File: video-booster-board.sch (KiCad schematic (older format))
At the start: 129 parts, among them IC1 INA180A1IDBVT, J1 0473460001, J10 M20-9990246, J11 MC-HVT1-S04-G, J2 HDMI-PE10-19-LF, J3 HDMI-PE10-19-LF, J6 685119134923_, J9 685119134923_, SW1 1571983-5, U1 PTN3363, U2 TPS2110APW, U3 PTN3363, U4 LP2985-33DBVR, U5 NTS0102GT, U6 EFM32HG321, U7 NTS0102GT

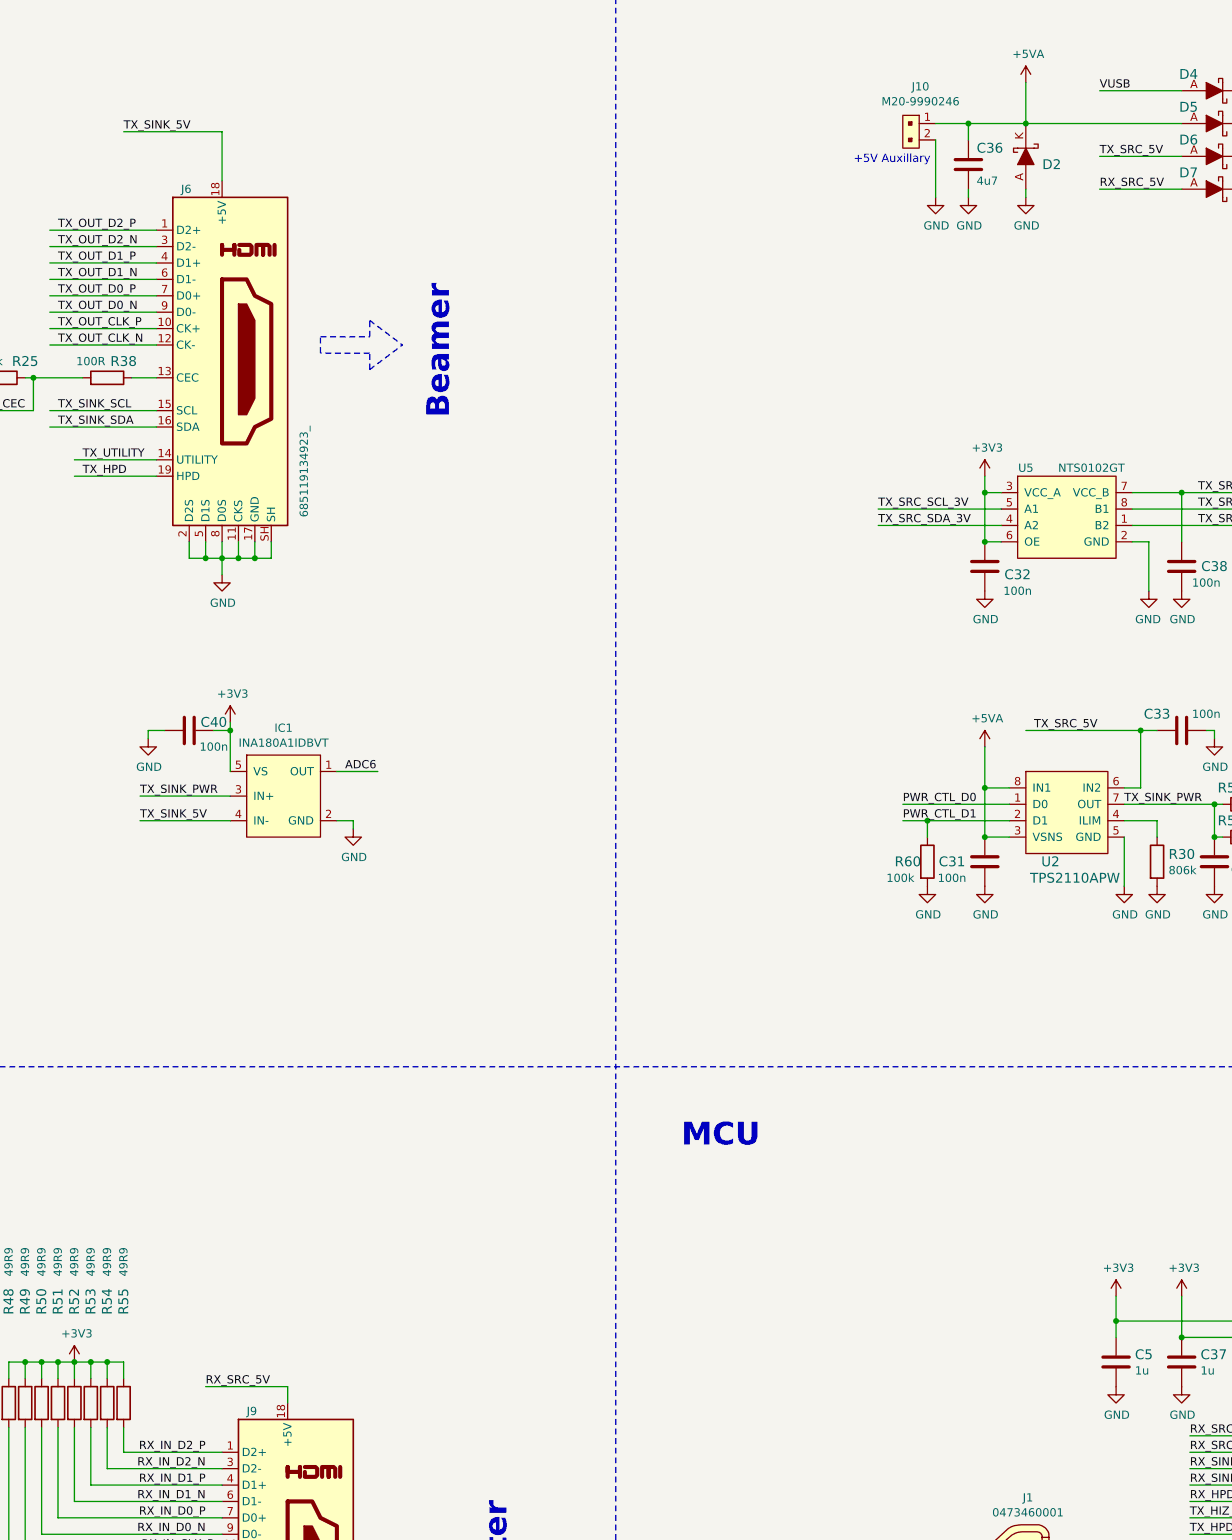
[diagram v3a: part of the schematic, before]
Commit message: Additional decoupling on MCU adn TX_SINK_5V added
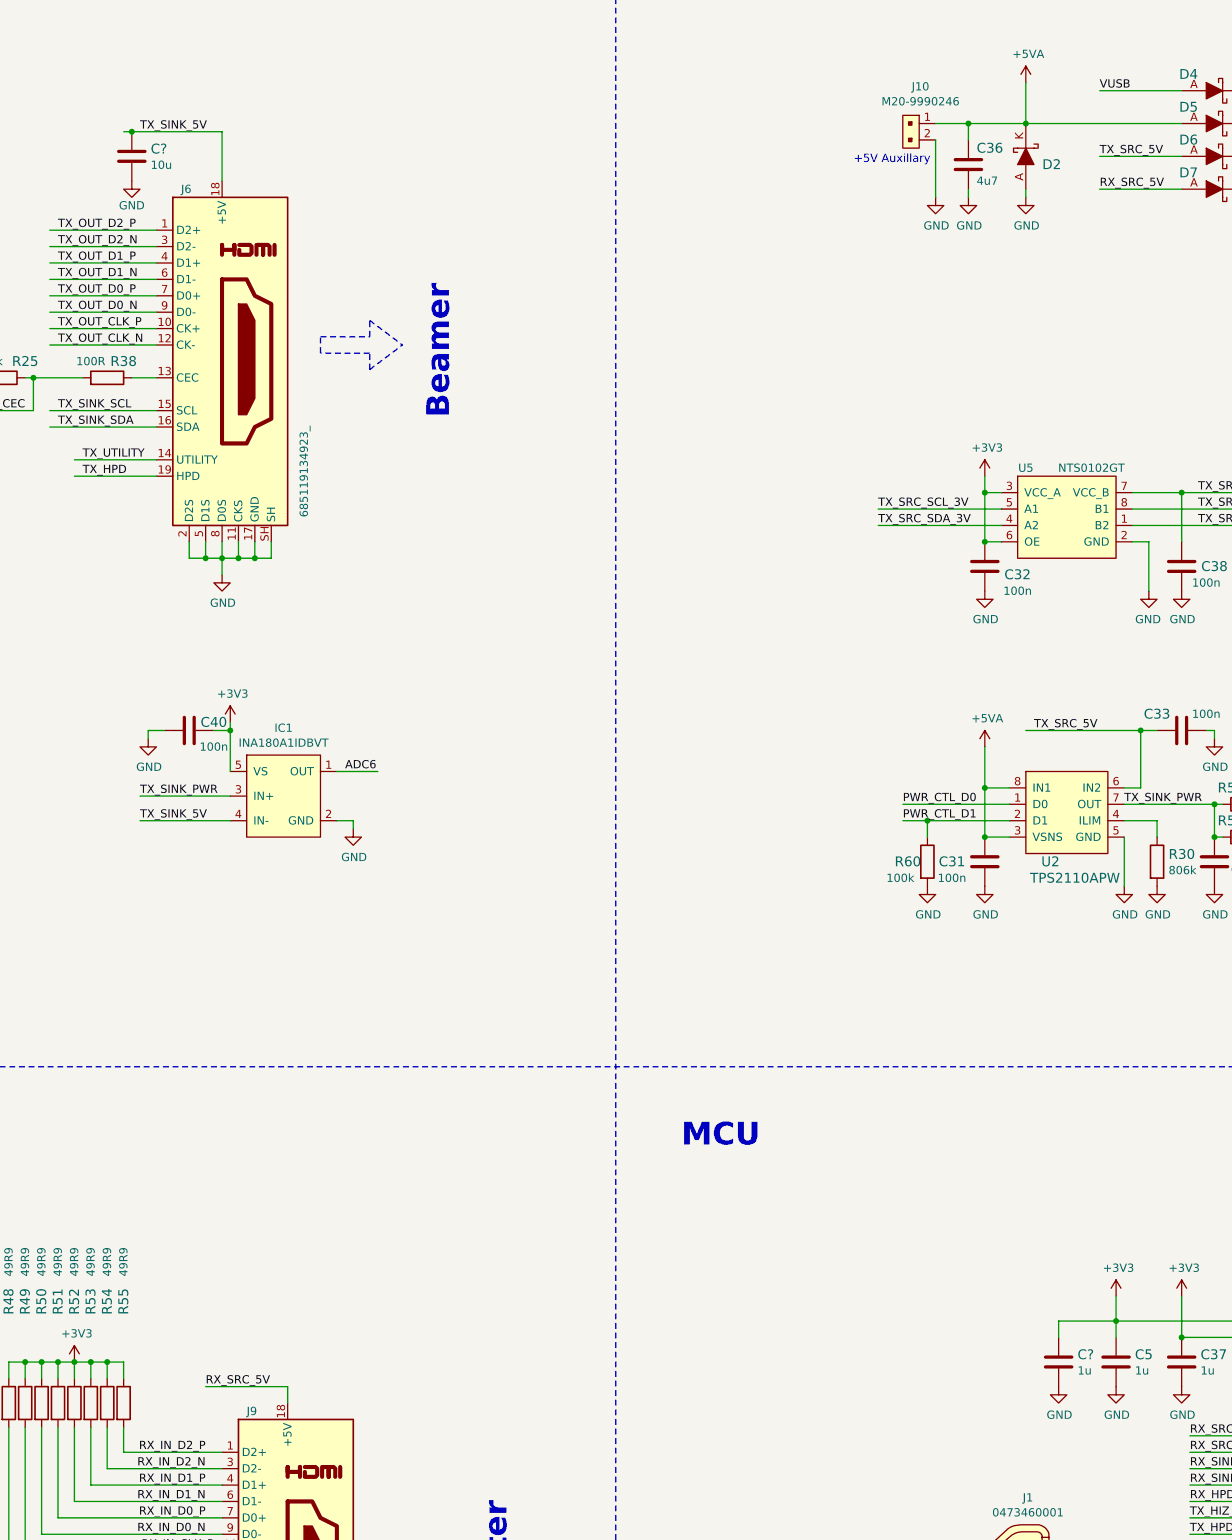
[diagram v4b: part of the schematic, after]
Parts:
- added C?: C_1u_0402, video-booster-board-footprints:0402-cap, symbol video-booster-board:C_1u_0402-
- added C?: C_10u_0603, video-booster-board-footprints:0603-cap, symbol video-booster-board:C_10u_0603-
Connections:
- wire segments 564 -> 567
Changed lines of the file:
@@
 Wire Wire Line
 	16800 5950 17350 5950
-Text Label 9750 1850 0    50   ~ 0
+Text Label 9850 1850 0    50   ~ 0
 TX_SINK_5V
 Wire Wire Line
-	10350 1850 9750 1850
+	10350 1850 9800 1850
 Wire Notes Line
 	12800 13000 22950 13000
@@
 Wire Wire Line
 	16850 10300 16250 10300
+$Comp
+L video-booster-board:C_1u_0402- C?
+U 1 1 5DE6659D
+P 15450 9350
+F 0 "C?" H 15565 9395 60  0000 L CNN
+F 1 "C_1u_0402" H 15450 9200 60  0001 C CNN
+F 2 "video-booster-board-footprints:0402-cap" H 15650 9550 60  0001 L CNN
+F 3 "" H 15450 9350 50  0001 C CNN
+F 4 "TDK" H 15650 9750 60  0001 L CNN "Manufacturer"
+F 5 "C1005X6S1A105K050BC" H 15650 9650 60  0001 L CNN "MPN"
+F 6 "1u" H 15565 9297 50  0000 L CNN "Val"
+	1    15450 9350
+	1    0    0    -1
+$EndComp
+$Comp
+L video-booster-board:GND #PWR?
+U 1 1 5DE668F7
+P 15450 9500
+F 0 "#PWR?" H 15450 9250 50  0001 C CNN
+F 1 "GND" H 15455 9327 50  0000 C CNN
+F 2 "" H 15450 9500 50  0001 C CNN
+F 3 "" H 15450 9500 50  0001 C CNN
+	1    15450 9500
+	1    0    0    -1
+$EndComp
+Wire Wire Line
+	15800 9100 15450 9100
+Wire Wire Line
+	15450 9100 15450 9200
+$Comp
+L video-booster-board:C_10u_0603- C?
+U 1 1 5DED3A14
+P 9800 2000
+F 0 "C?" H 9915 2045 60  0000 L CNN
+F 1 "C_10u_0603" H 9800 1850 60  0001 C CNN
+F 2 "video-booster-board-footprints:0603-cap" H 10000 2200 60  0001 L CNN
+F 3 "" H 9800 2000 50  0001 C CNN
+F 4 "AVX" H 10000 2400 60  0001 L CNN "Manufacturer"
+F 5 "06036D106MAT2A" H 10000 2300 60  0001 L CNN "MPN"
+F 6 "10u" H 9915 1947 50  0000 L CNN "Val"
+	1    9800 2000
+	1    0    0    -1
+$EndComp
+Connection ~ 9800 1850
+Wire Wire Line
+	9800 1850 9750 1850
+$Comp
+L video-booster-board:GND #PWR?
+U 1 1 5DED892B
+P 9800 2150
+F 0 "#PWR?" H 9800 1900 50  0001 C CNN
+F 1 "GND" H 9800 2000 50  0000 C CNN
+F 2 "" H 9800 2150 50  0001 C CNN
+F 3 "" H 9800 2150 50  0001 C CNN
+	1    9800 2150
+	1    0    0    -1
+$EndComp
 $EndSCHEMATC

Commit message: OSHW logo and board name added on PCB
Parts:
- added N1: oshw_logo, video-booster-board-footprints:OSHW-Logo2_7.3x6mm_Copper_Mask, symbol video-booster-board:oshw_logo
- gave numbers to parts that had none: 2
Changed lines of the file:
@@
 TX_HIZ_EN
 $Bitmap
-Pos 2300 15650
+Pos 19400 15100
 Scale 1.000000
 Data
@@
 RX_SINK_CEC
 $Bitmap
-Pos 1100 15650
+Pos 22500 15100
 Scale 0.850000
 Data
@@
 	16850 10300 16250 10300
 $Comp
-L video-booster-board:C_1u_0402- C?
+L video-booster-board:C_1u_0402- C42
 U 1 1 5DE6659D
 P 15450 9350
-F 0 "C?" H 15565 9395 60  0000 L CNN
+F 0 "C42" H 15565 9395 60  0000 L CNN
 F 1 "C_1u_0402" H 15450 9200 60  0001 C CNN
 F 2 "video-booster-board-footprints:0402-cap" H 15650 9550 60  0001 L CNN
@@
 $EndComp
 $Comp
-L video-booster-board:GND #PWR?
+L video-booster-board:GND #PWR026
 U 1 1 5DE668F7
 P 15450 9500
-F 0 "#PWR?" H 15450 9250 50  0001 C CNN
+F 0 "#PWR026" H 15450 9250 50  0001 C CNN
 F 1 "GND" H 15455 9327 50  0000 C CNN
 F 2 "" H 15450 9500 50  0001 C CNN
@@
 	15450 9100 15450 9200
 $Comp
-L video-booster-board:C_10u_0603- C?
+L video-booster-board:C_10u_0603- C41
 U 1 1 5DED3A14
 P 9800 2000
-F 0 "C?" H 9915 2045 60  0000 L CNN
+F 0 "C41" H 9915 2045 60  0000 L CNN
 F 1 "C_10u_0603" H 9800 1850 60  0001 C CNN
 F 2 "video-booster-board-footprints:0603-cap" H 10000 2200 60  0001 L CNN
@@
 	9800 1850 9750 1850
 $Comp
-L video-booster-board:GND #PWR?
+L video-booster-board:GND #PWR021
 U 1 1 5DED892B
 P 9800 2150
-F 0 "#PWR?" H 9800 1900 50  0001 C CNN
+F 0 "#PWR021" H 9800 1900 50  0001 C CNN
 F 1 "GND" H 9800 2000 50  0000 C CNN
 F 2 "" H 9800 2150 50  0001 C CNN
@@
 	1    0    0    -1
 $EndComp
+$Comp
+L video-booster-board:oshw_logo N1
+U 1 1 5DF48A15
+P 22350 13450
+F 0 "N1" H 22100 13800 50  0000 L CNN
+F 1 "oshw_logo" H 22100 13700 50  0000 L CNN
+F 2 "video-booster-board-footprints:OSHW-Logo2_7.3x6mm_Copper_Mask" H 22250 13700 50  0001 C CNN
+F 3 "" H 22350 13800 50  0001 C CNN
+	1    22350 13450
+	1    0    0    -1
+$EndComp

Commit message: Updated sections
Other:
- note added: "Markings"
- note added: "TBD: Consider changing into a small barrel jack (SMT)"
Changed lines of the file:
@@
 TX_HIZ_EN
 $Bitmap
-Pos 19400 15100
+Pos 1400 15650
 Scale 1.000000
 Data
@@
 	1    0    0    -1
 $EndComp
-Text Notes 14200 2050 0    50   ~ 0
+Text Notes 14000 1850 0    50   ~ 0
 +5V Auxillary
 $Comp
@@
 RX_SINK_CEC
 $Bitmap
-Pos 22500 15100
+Pos 2600 15650
 Scale 0.850000
 Data
@@
 L video-booster-board:oshw_logo N1
 U 1 1 5DF48A15
-P 22350 13450
-F 0 "N1" H 22100 13800 50  0000 L CNN
-F 1 "oshw_logo" H 22100 13700 50  0000 L CNN
-F 2 "video-booster-board-footprints:OSHW-Logo2_7.3x6mm_Copper_Mask" H 22250 13700 50  0001 C CNN
-F 3 "" H 22350 13800 50  0001 C CNN
-	1    22350 13450
+P 18900 14250
+F 0 "N1" H 18650 14600 50  0000 L CNN
+F 1 "oshw_logo" H 18650 14500 50  0000 L CNN
+F 2 "video-booster-board-footprints:OSHW-Logo2_7.3x6mm_Copper_Mask" H 18800 14500 50  0001 C CNN
+F 3 "" H 18900 14600 50  0001 C CNN
+	1    18900 14250
 	1    0    0    -1
 $EndComp
+Text Notes 13600 2650 0    50   ~ 0
+TBD: Consider changing into a small barrel jack (SMT)
+Wire Notes Line
+	17650 13000 17650 16050
+Text Notes 17800 13350 0    138  ~ 28
+Markings
 $EndSCHEMATC

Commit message: Opsis side HDMI connector type changed. Board shape adjusted, DC jack added
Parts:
- removed J2, J3: HDMI-PE10-19-LF, video-booster-board-footprints:HDMI-PE10-19-LF, symbol video-booster-board:HDMI-PE10-19-LF-
- removed J6, J9: 685119134923_, video-booster-board-footprints:HDMI_A_Female_685119134923, symbol video-booster-board:685119134923_-
- added J2, J3: CHDMI-AMSS-01-C, video-booster-board-footprints:CHDMI-AMSS-01-C, symbol video-booster-board:CHDMI-AMSS-01-C
- added J4: 694103107102, video-booster-board-footprints:69410X107102, symbol video-booster-board:694103107102
- added J6, J9: 685119134923_, video-booster-board-footprints:HDMI_A_Female_685119134923, symbol video-booster-board:685119134923_
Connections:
- wire segments 567 -> 572
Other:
- note removed: "TBD: Consider changing into a small barrel jack (SMT)"
- moved on the sheet: J10
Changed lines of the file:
@@
 $EndComp
 $Comp
-L video-booster-board:HDMI-PE10-19-LF- J2
-U 1 1 5DBAED87
-P 2100 3400
-F 0 "J2" V 1650 2650 50  0000 R CNN
-F 1 "HDMI-PE10-19-LF" V 1750 3300 50  0000 R CNN
-F 2 "video-booster-board-footprints:HDMI-PE10-19-LF" H 2300 3600 60  0001 L CNN
-F 3 "http://www.morethanall.com/images/products/March2017/JtPYSqVaIFqwSbTYDg6j.pdf" H 2175 3550 50  0001 C CNN
-	1    2100 3400
-	1    0    0    -1
-$EndComp
-$Comp
-L video-booster-board:685119134923_- J6
-U 1 1 5DBAFB0A
-P 10350 3250
-F 0 "J6" H 10100 4300 50  0000 L CNN
-F 1 "685119134923_" V 10850 2300 50  0000 L CNN
-F 2 "video-booster-board-footprints:HDMI_A_Female_685119134923" H 10550 3450 60  0001 L CNN
-F 3 "https://katalog.we-online.de/em/datasheet/685119134923.pdf" H 10375 3250 50  0001 C CNN
-	1    10350 3250
-	1    0    0    -1
-$EndComp
-$Comp
 L video-booster-board:C_100n_0402_6V3- C27
 U 1 1 5DBDC1F8
@@
 $EndComp
 $Comp
-L video-booster-board:HDMI-PE10-19-LF- J3
-U 1 1 5DF9B9E7
-P 2450 10850
-F 0 "J3" V 2000 10100 50  0000 R CNN
-F 1 "HDMI-PE10-19-LF" V 2100 10750 50  0000 R CNN
-F 2 "video-booster-board-footprints:HDMI-PE10-19-LF" H 2650 11050 60  0001 L CNN
-F 3 "http://www.morethanall.com/images/products/March2017/JtPYSqVaIFqwSbTYDg6j.pdf" H 2525 11000 50  0001 C CNN
-	1    2450 10850
-	1    0    0    -1
-$EndComp
-$Comp
-L video-booster-board:685119134923_- J9
-U 1 1 5DF9B9EE
-P 10750 10700
-F 0 "J9" H 10500 11750 50  0000 L CNN
-F 1 "685119134923_" V 11250 9750 50  0000 L CNN
-F 2 "video-booster-board-footprints:HDMI_A_Female_685119134923" H 10950 10900 60  0001 L CNN
-F 3 "https://katalog.we-online.de/em/datasheet/685119134923.pdf" H 10775 10700 50  0001 C CNN
-	1    10750 10700
-	1    0    0    -1
-$EndComp
-$Comp
 L video-booster-board:PTN3363- U1
 U 1 1 5DF9BA02
@@
 TX_SINK_SCL_3V
 $Comp
-L video-booster-board:C_4u7_0603- C36
-U 1 1 62A47AFC
-P 14900 2050
-F 0 "C36" H 14950 2150 60  0000 L CNN
-F 1 "C_4u7_0603" H 14900 1900 60  0001 C CNN
-F 2 "video-booster-board-footprints:0603-cap" H 15100 2250 60  0001 L CNN
-F 3 "" H 14900 2050 50  0001 C CNN
-F 4 "TDK" H 15100 2450 60  0001 L CNN "Manufacturer"
-F 5 "C1608X5R1V475M080AC" H 15100 2350 60  0001 L CNN "MPN"
-F 6 "4u7" H 14950 1950 50  0000 L CNN "Val"
-	1    14900 2050
-	1    0    0    -1
-$EndComp
-$Comp
-L video-booster-board:GND #PWR061
-U 1 1 62AD30B5
-P 14700 2250
-F 0 "#PWR061" H 14700 2000 50  0001 C CNN
-F 1 "GND" H 14705 2077 50  0000 C CNN
-F 2 "" H 14700 2250 50  0001 C CNN
-F 3 "" H 14700 2250 50  0001 C CNN
-	1    14700 2250
-	1    0    0    -1
-$EndComp
-$Comp
-L video-booster-board:GND #PWR062
-U 1 1 62AD3480
-P 14900 2250
-F 0 "#PWR062" H 14900 2000 50  0001 C CNN
-F 1 "GND" H 14905 2077 50  0000 C CNN
-F 2 "" H 14900 2250 50  0001 C CNN
-F 3 "" H 14900 2250 50  0001 C CNN
-	1    14900 2250
-	1    0    0    -1
-$EndComp
-$Comp
 L video-booster-board:GND #PWR068
 U 1 1 62AD35F3
@@
 	1    0    0    -1
 $EndComp
-Text Notes 14000 1850 0    50   ~ 0
-+5V Auxillary
 $Comp
 L video-booster-board:+5VA #PWR036
@@
 $EndComp
 Wire Wire Line
-	14700 2250 14700 1900
-Wire Wire Line
-	14700 1800 14900 1800
-Wire Wire Line
 	15250 1550 15250 1800
 Connection ~ 15250 1800
 Wire Wire Line
-	14900 1800 14900 1900
-Connection ~ 14900 1800
-Wire Wire Line
-	14900 1800 15250 1800
-Wire Wire Line
-	14900 2200 14900 2250
-Wire Wire Line
 	15250 2200 15250 2250
 $Comp
@@
 L video-booster-board:M20-9990246 J10
 U 1 1 5DD74C13
-P 14600 1800
-F 0 "J10" V 14375 1808 50  0000 C CNN
-F 1 "M20-9990246" V 14466 1808 50  0000 C CNN
-F 2 "video-booster-board-footprints:PinHeader_1x2_P2.54mm" H 14800 2000 60  0001 L CNN
-F 3 "https://cdn.harwin.com/pdfs/M20-999.pdf" H 14800 2100 60  0001 L CNN
-F 4 "M20-9990246" H 14800 2300 60  0001 L CNN "MPN"
-F 5 "Harwin Inc." H 14800 2900 60  0001 L CNN "Manufacturer"
-	1    14600 1800
+P 14500 2000
+F 0 "J10" V 14000 2000 50  0000 C CNN
+F 1 "M20-9990246" V 14100 2100 50  0000 C CNN
+F 2 "video-booster-board-footprints:PinHeader_1x2_P2.54mm" H 14700 2200 60  0001 L CNN
+F 3 "https://cdn.harwin.com/pdfs/M20-999.pdf" H 14700 2300 60  0001 L CNN
+F 4 "M20-9990246" H 14700 2500 60  0001 L CNN "MPN"
+F 5 "Harwin Inc." H 14700 3100 60  0001 L CNN "Manufacturer"
+	1    14500 2000
 	0    1    1    0
 $EndComp
@@
 	1    0    0    -1
 $EndComp
-Text Notes 13600 2650 0    50   ~ 0
-TBD: Consider changing into a small barrel jack (SMT)
 Wire Notes Line
 	17650 13000 17650 16050
 Text Notes 17800 13350 0    138  ~ 28
 Markings
+$Comp
+L video-booster-board:CHDMI-AMSS-01-C J2
+U 1 1 5DE81C03
+P 2100 3400
+F 0 "J2" V 1650 2650 50  0000 R CNN
+F 1 "CHDMI-AMSS-01-C" V 1750 3300 50  0000 R CNN
+F 2 "video-booster-board-footprints:CHDMI-AMSS-01-C" H 2300 3600 60  0001 L CNN
+F 3 "" H 2175 3550 50  0001 C CNN
+	1    2100 3400
+	1    0    0    -1
+$EndComp
+$Comp
+L video-booster-board:CHDMI-AMSS-01-C J3
+U 1 1 5DE89759
+P 2450 10850
+F 0 "J3" V 2000 10100 50  0000 R CNN
+F 1 "CHDMI-AMSS-01-C" V 2100 10750 50  0000 R CNN
+F 2 "video-booster-board-footprints:CHDMI-AMSS-01-C" H 2650 11050 60  0001 L CNN
+F 3 "" H 2525 11000 50  0001 C CNN
+	1    2450 10850
+	1    0    0    -1
+$EndComp
+Wire Wire Line
+	14900 2200 14900 2250
+Wire Wire Line
+	14900 1800 15250 1800
+Wire Wire Line
+	14900 1800 14900 1900
+Wire Wire Line
+	14150 1800 14600 1800
+Text Notes 13550 2150 0    50   ~ 0
++5V Auxillary
+$Comp
+L video-booster-board:GND #PWR062
+U 1 1 62AD3480
+P 14900 2250
+F 0 "#PWR062" H 14900 2000 50  0001 C CNN
+F 1 "GND" H 14905 2077 50  0000 C CNN
+F 2 "" H 14900 2250 50  0001 C CNN
+F 3 "" H 14900 2250 50  0001 C CNN
+	1    14900 2250
+	1    0    0    -1
+$EndComp
+$Comp
+L video-booster-board:GND #PWR061
+U 1 1 62AD30B5
+P 14150 2250
+F 0 "#PWR061" H 14150 2000 50  0001 C CNN
+F 1 "GND" H 14155 2077 50  0000 C CNN
+F 2 "" H 14150 2250 50  0001 C CNN
+F 3 "" H 14150 2250 50  0001 C CNN
+	1    14150 2250
+	1    0    0    -1
+$EndComp
+$Comp
+L video-booster-board:C_4u7_0603- C36
+U 1 1 62A47AFC
+P 14900 2050
+F 0 "C36" H 14950 2150 60  0000 L CNN
+F 1 "C_4u7_0603" H 14900 1900 60  0001 C CNN
+F 2 "video-booster-board-footprints:0603-cap" H 15100 2250 60  0001 L CNN
+F 3 "" H 14900 2050 50  0001 C CNN
+F 4 "TDK" H 15100 2450 60  0001 L CNN "Manufacturer"
+F 5 "C1608X5R1V475M080AC" H 15100 2350 60  0001 L CNN "MPN"
+F 6 "4u7" H 14950 1950 50  0000 L CNN "Val"
+	1    14900 2050
+	1    0    0    -1
+$EndComp
+Connection ~ 14900 1800
+Wire Wire Line
+	14600 1800 14600 2000
+Connection ~ 14600 1800
+Wire Wire Line
+	14600 1800 14900 1800
+Wire Wire Line
+	14600 2100 14600 2250
+$Comp
+L video-booster-board:GND #PWR090
+U 1 1 5E16E7E8
+P 14600 2250
+F 0 "#PWR090" H 14600 2000 50  0001 C CNN
+F 1 "GND" H 14605 2077 50  0000 C CNN
+F 2 "" H 14600 2250 50  0001 C CNN
+F 3 "" H 14600 2250 50  0001 C CNN
+	1    14600 2250
+	1    0    0    -1
+$EndComp
+$Comp
+L video-booster-board:685119134923_ J6
+U 1 1 5E191611
+P 10350 3250
+F 0 "J6" H 10100 4300 50  0000 L CNN
+F 1 "685119134923_" V 10800 2250 50  0000 L CNN
+F 2 "video-booster-board-footprints:HDMI_A_Female_685119134923" H 10550 3450 60  0001 L CNN
+F 3 "https://katalog.we-online.de/em/datasheet/685119134923.pdf" H 10375 3250 50  0001 C CNN
+	1    10350 3250
+	1    0    0    -1
+$EndComp
+$Comp
+L video-booster-board:685119134923_ J9
+U 1 1 5E1A9DA9
+P 10750 10700
+F 0 "J9" H 10500 11750 50  0000 L CNN
+F 1 "685119134923_" V 11200 9700 50  0000 L CNN
+F 2 "video-booster-board-footprints:HDMI_A_Female_685119134923" H 10950 10900 60  0001 L CNN
+F 3 "https://katalog.we-online.de/em/datasheet/685119134923.pdf" H 10775 10700 50  0001 C CNN
+	1    10750 10700
+	1    0    0    -1
+$EndComp
+Wire Wire Line
+	14150 1900 14150 2000
+Wire Wire Line
+	14150 2000 14150 2250
+Connection ~ 14150 2000
+$Comp
+L video-booster-board:694103107102 J4
+U 1 1 5DECDCEC
+P 14150 1800
+F 0 "J4" H 13950 2100 50  0000 C CNN
+F 1 "694103107102" H 13950 2000 50  0000 C CNN
+F 2 "video-booster-board-footprints:69410X107102" H 14350 1825 50  0001 L BNN
+F 3 "https://www.we-online.de/katalog/datasheet/694103107102.pdf" H 14350 1600 50  0001 L BNN
+F 4 "None" H 14350 1750 50  0001 L BNN "Field4"
+F 5 "694103107102" H 14350 1675 50  0001 L BNN "Field5"
+F 6 "Unavailable" H 14350 1450 50  0001 L BNN "Field6"
+F 7 "Wurth Electronics" H 14350 1525 50  0001 L BNN "Field7"
+F 8 "DC Power jack" H 14350 1875 50  0001 L BNN "Field8"
+	1    14150 1800
+	1    0    0    -1
+$EndComp
+Wire Wire Line
+	14150 1800 14150 1725
+Connection ~ 14150 1800
 $EndSCHEMATC
